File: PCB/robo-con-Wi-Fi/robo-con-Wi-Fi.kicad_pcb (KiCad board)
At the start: 4 copper layers, 86 x 67 mm, 121 parts, among them J1 Conn_01x04, J2 SMA-J, J3 Conn_01x05, J4 Conn_01x01, J5 Conn_01x02, J6 Conn_01x01, J7 Conn_01x06, Q1 2SC3325-Y, SW1 SW_Push, SW2 SW_Push, U1 STM32H723VGTx, U10 MCP73831-2-OT, U11 LM66100DCK, U12 NJM12877, U13 TXB0606DYYR, U14 TPS628513DRLR, U15 LM66100DCK, U18 USB_Type-C, U2 LBEE5HY2FY, U3 TXU0204, U5 RKJXV122400R, U6 IS25LP064D-JLLE, U7 RKJXV122400R, U8 TMHU28, U9 TMHU28, Y2 XRCGB25M000FFS1AR0

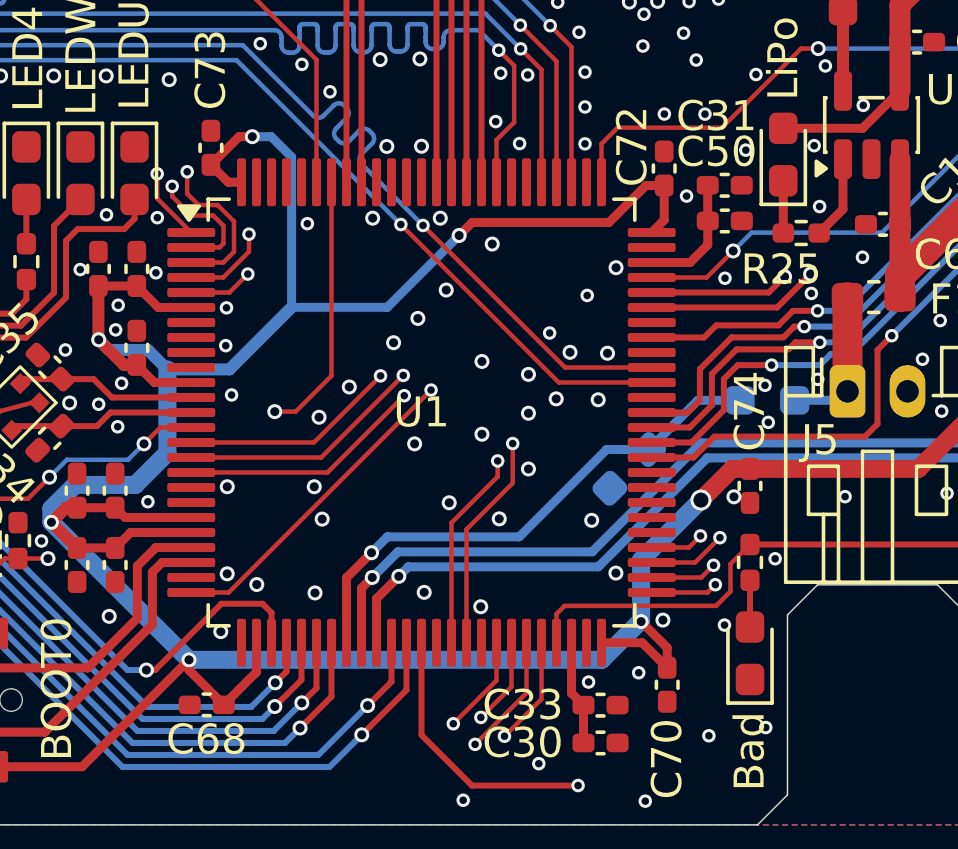
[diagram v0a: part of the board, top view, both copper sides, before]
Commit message: sdioのプルアップ追加
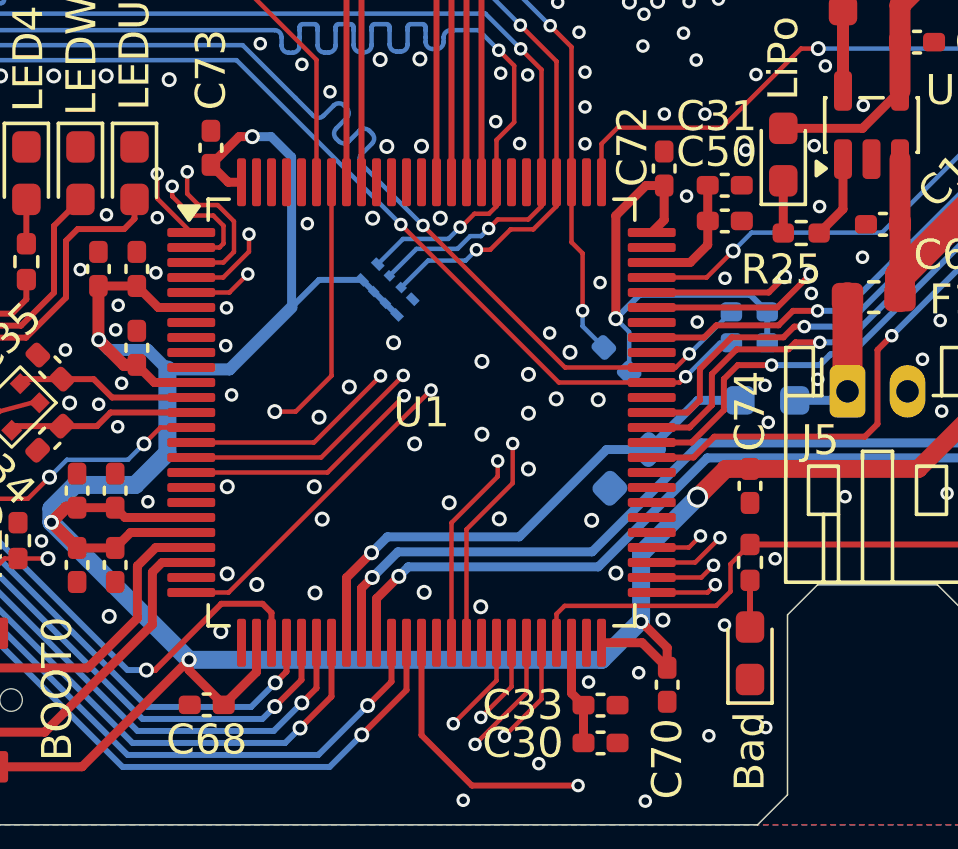
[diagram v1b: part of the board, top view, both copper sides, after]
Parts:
- added R44: WA04X102, My_Library:WA04X102, B.Cu at (169.7, 72.2)
- added R45: 1k, Resistor_SMD:R_0402_1005Metric_Pad0.72x0.64mm_HandSolder, B.Cu at (181.7, 73.9)
- added R46: 1k, Resistor_SMD:R_0402_1005Metric_Pad0.72x0.64mm_HandSolder, B.Cu at (181.7, 72.9)
- added R47: 1k, Resistor_SMD:R_0402_1005Metric_Pad0.72x0.64mm_HandSolder, B.Cu at (177.3, 74.5)
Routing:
- net +3.3V: track 459.6 -> 471.2 mm
- net SDMMC1_D3: track 60.6 -> 67.7 mm, vias 2 -> 3
- net SDMMC1_CLK: track 60.7 -> 67.5 mm, vias 2 -> 3
- net SDMMC1_D2: track 60.8 -> 66.7 mm, vias 2 -> 3
- net SDMMC1_CMD: track 60.8 -> 66.3 mm, vias 2 -> 3
- net SDMMC1_D1: track 60.8 -> 64.2 mm, vias 2 -> 3
- net SDMMC1_D0: track 60.9 -> 64.1 mm, vias 2 -> 3
- net GND: vias 535 -> 530

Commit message: ガーバー出力
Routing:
- net GND: vias 530 -> 531
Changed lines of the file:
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@@
+	)
+	(via
+		(at 171.660048 72.173554)
+		(size 0.45)
+		(drill 0.25)
+		(layers "F.Cu" "B.Cu")
+		(free yes)
+		(net "GND")
 	)
 	(via
